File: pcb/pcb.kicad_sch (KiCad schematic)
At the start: 182 parts, among them J1 USB_C_Receptacle_USB2.0_14P, J2 Conn_01x04_Pin, J3 Conn_01x04_Pin, J4 Conn_01x04_Socket, J5 Conn_01x02_Pin, Q1 BSS84, SW1 SW_Push, SW10(8) SW_Push_45deg, SW11(9) SW_Push_45deg, SW12(0) SW_Push_45deg, SW13(-) SW_Push_45deg, SW14(=) SW_Push_45deg, SW15(bckspc) SW_Push_45deg, SW16(tab) SW_Push_45deg, SW17(q) SW_Push_45deg, SW18(w) SW_Push_45deg, SW19(e) SW_Push_45deg, SW2(esc) SW_Push_45deg, SW20(r) SW_Push_45deg, SW21(t) SW_Push_45deg, SW22(y) SW_Push_45deg, SW23(u) SW_Push_45deg, SW24(i) SW_Push_45deg, SW25(o) SW_Push_45deg, SW26(p) SW_Push_45deg, SW27([) SW_Push_45deg, SW28(]) SW_Push_45deg, SW29(\) SW_Push_45deg, SW3(1) SW_Push_45deg, SW30(caps) SW_Push_45deg, SW31(unused) SW_Push_45deg, SW32(a) SW_Push_45deg, SW33(lshift) SW_Push_45deg, SW34(s) SW_Push_45deg, SW35(z) SW_Push_45deg, SW36(d) SW_Push_45deg, SW37(x) SW_Push_45deg, SW38(f) SW_Push_45deg, SW39(c) SW_Push_45deg, SW4(2) SW_Push_45deg, SW40(g) SW_Push_45deg, SW41(v) SW_Push_45deg, SW42(h) SW_Push_45deg, SW43(b) SW_Push_45deg, SW44(j) SW_Push_45deg, SW45(n) SW_Push_45deg, SW46(k) SW_Push_45deg, SW47(m) SW_Push_45deg, SW48(l) SW_Push_45deg, SW49(,) SW_Push_45deg, SW5(3) SW_Push_45deg, SW50(;) SW_Push_45deg, SW51(.) SW_Push_45deg, SW52(') SW_Push_45deg, SW53(/) SW_Push_45deg, SW54(ret) SW_Push_45deg, SW55(rshift) SW_Push_45deg, SW56(unused) SW_Push_45deg, SW57(up) SW_Push_45deg, SW58(globe) SW_Push_45deg, SW6(4) SW_Push_45deg, SW60(lctrl) SW_Push_45deg, SW62(super) SW_Push_45deg, SW64(lalt) SW_Push_45deg, SW66(spc) SW_Push_45deg, SW68(spc) SW_Push_45deg, SW7(5) SW_Push_45deg, SW70(spc) SW_Push_45deg, SW72(spc) SW_Push_45deg, SW74(spc) SW_Push_45deg, SW76(ralt) SW_Push_45deg, SW78(rctrl) SW_Push_45deg, SW8(6) SW_Push_45deg, SW80(left) SW_Push_45deg, SW82(down) SW_Push_45deg, SW84(right) SW_Push_45deg, SW9(7) SW_Push_45deg, U1 ESP32-C3-WROOM-02, U2 AP2112K-3.3, U3 TCA6424ARGJR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

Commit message: add nc flag to nc pins on symbol and most importantly, connect all the necessary components to get the touchic funcitoning (ATMXT1664T3-CCUR035 136-ball bga version)
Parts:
- removed J3: Conn_01x04_Pin, symbol Connector:Conn_01x04_Pin
- removed SW10(8): SW_Push_45deg, symbol Switch:SW_Push_45deg
- added C10, C13, C14, C16, C6: 2.2uF, symbol Device:C
- added C11, C12, C15, C17: 22nF, symbol Device:C
- added C7, C9: 100nF, symbol Device:C
- added C8: 10nF, symbol Device:C
- added R27, R28, R29: R, symbol Device:R
- added R30: 100k, symbol Device:R
- added R31: 3.3k, symbol Device:R
- added R32: 10k, symbol Device:R
- added SW10(8)1: SW_Push_45deg, symbol Switch:SW_Push_45deg
- added SW2, SW3, SW4: SW_Push, symbol Switch:SW_Push
- added U5: ~, footprints:UFBGA136_MCH-M, symbol 2025-08-11_22-50-31:The_Touch_IC
- renumbered SW11(9) to SW11(9)1, SW12(0) to SW12(0)1, SW13(-) to SW13(-)1, SW14(=) to SW14(=)1, SW15(bckspc) to SW15(bckspc)1, SW16(tab) to SW16(tab)1, SW17(q) to SW17(q)1, SW18(w) to SW18(w)1, SW19(e) to SW19(e)1, SW2(esc) to SW2(esc)1, SW20(r) to SW20(r)1, SW21(t) to SW21(t)1, SW22(y) to SW22(y)1, SW23(u) to SW23(u)1, SW24(i) to SW24(i)1, SW25(o) to SW25(o)1, SW26(p) to SW26(p)1, SW27([) to SW27([)1, SW28(]) to SW28(])1, SW29(\) to SW29(\)1, SW3(1) to SW3(1)1, SW30(caps) to SW30(caps)1, SW31(unused) to SW31(unused)1, SW32(a) to SW32(a)1, SW33(lshift) to SW33(lshift)1, SW34(s) to SW34(s)1, SW35(z) to SW35(z)1, SW36(d) to SW36(d)1, SW37(x) to SW37(x)1, SW38(f) to SW38(f)1, SW39(c) to SW39(c)1, SW4(2) to SW4(2)1, SW40(g) to SW40(g)1, SW41(v) to SW41(v)1, SW42(h) to SW42(h)1, SW43(b) to SW43(b)1, SW44(j) to SW44(j)1, SW45(n) to SW45(n)1, SW46(k) to SW46(k)1, SW47(m) to SW47(m)1, SW48(l) to SW48(l)1, SW49(,) to SW49(,)1, SW5(3) to SW5(3)1, SW50(;) to SW50(;)1, SW51(.) to SW51(.)1, SW52(') to SW52(')1, SW53(/) to SW53(/)1, SW54(ret) to SW54(ret)1, SW55(rshift) to SW55(rshift)1, SW56(unused) to SW56(unused)1, SW57(up) to SW57(up)1, SW58(globe) to SW58(globe)1, SW6(4) to SW6(4)1, SW60(lctrl) to SW60(lctrl)1, SW62(super) to SW62(super)1, SW64(lalt) to SW64(lalt)1, SW66(spc) to SW66(spc)1, SW68(spc) to SW68(spc)1, SW7(5) to SW7(5)1, SW70(spc) to SW70(spc)1, SW72(spc) to SW72(spc)1, SW74(spc) to SW74(spc)1, SW76(ralt) to SW76(ralt)1, SW78(rctrl) to SW78(rctrl)1, SW8(6) to SW8(6)1, SW80(left) to SW80(left)1, SW82(down) to SW82(down)1, SW84(right) to SW84(right)1, SW9(7) to SW9(7)1
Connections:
- net +3.3V: now also U3.27 (VCCP), C12.1, C13.1, SW2.2, SW3.2, SW4.2, U5.N6 (VDD)
- net Column 9: now also SW10(8)1.1
- net GND: now also C10.2, C11.2, C12.2, C13.2, C14.1, C15.1, C16.1, C17.1, C6.2, C7.2, C8.2, C9.2, R27.1, R28.1, R29.1, U5.A8 (GND), U5.C1 (GND), U5.C2 (GND), U5.D11 (GND), U5.D12 (GND), U5.D3 (GND), U5.F8 (GND), U5.K5 (USB_DM), U5.K7 (GND), U5.L4 (GND), U5.L6 (COMMSEL), U5.M10 (GND), U5.M4 (GND)
- net SCL: now also U5.M5 (SCL)
- net SDA: now also U5.L5 (SDA)
- net VBUS: now also C1.1, J1.A4 (VBUS), J1.A9 (VBUS), J1.B4 (VBUS), J1.B9 (VBUS), U2.1 (VIN), U2.3 (EN)
- net at D9.2 (A): now also SW10(8)1.2
- net at U3.15 (P16): now also R29.2, SW2.1
- net at U3.16 (P17): now also R28.2, SW3.1
- net at U3.17 (P20): now also R27.2, SW4.1
- net DRV2605 renamed DRV2605_EN
- new net: C8.1, R30.2, U5.N5 (RESET#)
- new net: C10.1, C9.1, U5.D2 (VDDCORE), U5.N7 (VDDCORE)
- new net: R31.2, U5.G6 (CHG#)
- new net ADDSEL: U5.M6 (ADDSEL/USB_DP)
- new net AVDD: C14.2, C15.2, U5.D1 (AVDD), U5.D13 (AVDD), U5.E11 (AVDD), U5.E3 (AVDD), U5.N10 (AVDD), U5.N4 (AVDD)
- new net DBG_CLK: U5.L8 (DBG_CLK/XTAL_XIN)
- new net DBG_DATA: U5.H8 (DBG_DATA/XTAL_XOUT)
- new net DBG_SS#/TEST#: R32.2, U5.G8 (TEST#/DBG_SS#)
- new net DRIVEN_SHIELD: U5.H10 (DSO)
- new net GPIO0: U5.F6 (GPIO0)
- new net GPIO1: U5.M7 (GPIO1)
- new net GPIO2: U5.L7 (GPIO2)
- new net GPIO3: U5.H7 (GPIO3)
- new net GPIO4: U5.F7 (GPIO4)
- new net GPIO5: U5.M8 (GPIO5)
- new net I2C_MODE: U5.K6 (I2C_MODE)
- new net NOISE_IN: U5.H6 (NOISE_IN)
- new net VDDCORE: C6.1, C7.1
- new net VDDIO: C11.1, R30.1, R31.1, R32.1, U5.K4 (VDDIO), U5.N8 (VDDIO)
- new net VREGBOOST: U5.C13 (VREGBOOST)
- new net XVDD: C16.2, C17.2, U5.A7 (XVDD), U5.B1 (XVDD), U5.C12 (XVDD)
- no-connect marks 0 -> 1
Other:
- note added: "ATMXT1664T3-CCUR035"
- moved on the sheet: D1, D10, D11, D12, D13, D14, D15, D16, D17, D18, D19, D2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

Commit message: add all of the footprints
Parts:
- removed J1: USB_C_Receptacle_USB2.0_14P, symbol Connector:USB_C_Receptacle_USB2.0_14P
- added USB1: TYPE-C 16PIN 2MD(073), easyeda2kicad:USB-C-SMD_TYPE-C-6PIN-2MD-073, symbol easyeda2kicad:TYPE-C16PIN2MD(073)
- C1, C10, C11, C12, C13, C14, C15, C16, C17, C2, C3, C4, C5, C6, C7, C8, C9: footprint (none) -> Capacitor_SMD:C_0603_1608Metric_Pad1.08x0.95mm_HandSolder
- D1, D10, D11, D12, D13, D14, D15, D16, D17, D18, D19, D2, D20, D21, D22, D23, D24, D25, D26, D27, D28, D29, D3, D30, D31, D32, D33, D34, D35, D36, D37, D38, D39, D4, D40, D41, D42, D43, D44, D45, D46, D47, D48, D49, D5, D50, D51, D52, D53, D54, D55, D56, D57, D59, D6, D61, D63, D65, D67, D69, D7, D71, D73, D75, D77, D79, D8, D81, D83, D9: footprint (none) -> Diode_SMD:D_SOD-523
- J2, J4: footprint (none) -> Connector_PinHeader_2.54mm:PinHeader_1x04_P2.54mm_Vertical
- J5: footprint (none) -> Connector_PinHeader_2.54mm:PinHeader_1x02_P2.54mm_Vertical
- R1, R10, R11, R12, R13, R14, R15, R16, R17, R18, R19, R2, R20, R21, R22, R23, R24, R25, R26, R3, R30, R31, R32, R4, R5, R6, R7, R8, R9: footprint (none) -> Resistor_SMD:R_1206_3216Metric_Pad1.30x1.75mm_HandSolder
- R27, R28, R29: value R -> 45k; footprint (none) -> Resistor_SMD:R_1206_3216Metric_Pad1.30x1.75mm_HandSolder
- SW1, SW2, SW3, SW4: footprint (none) -> Button_Switch_THT:SW_PUSH_6mm
- SW10(8)1, SW11(9)1, SW12(0)1, SW13(-)1, SW14(=)1, SW15(bckspc)1, SW16(tab)1, SW17(q)1, SW18(w)1, SW19(e)1, SW2(esc)1, SW20(r)1, SW21(t)1, SW22(y)1, SW23(u)1, SW24(i)1, SW25(o)1, SW26(p)1, SW27([)1, SW28(])1, SW29(\)1, SW3(1)1, SW30(caps)1, SW31(unused)1, SW32(a)1, SW33(lshift)1, SW34(s)1, SW35(z)1, SW36(d)1, SW37(x)1, SW38(f)1, SW39(c)1, SW4(2)1, SW40(g)1, SW41(v)1, SW42(h)1, SW43(b)1, SW44(j)1, SW45(n)1, SW46(k)1, SW47(m)1, SW48(l)1, SW49(,)1, SW5(3)1, SW50(;)1, SW51(.)1, SW52(')1, SW53(/)1, SW54(ret)1, SW55(rshift)1, SW56(unused)1, SW57(up)1, SW58(globe)1, SW6(4)1, SW60(lctrl)1, SW62(super)1, SW64(lalt)1, SW66(spc)1, SW68(spc)1, SW7(5)1, SW70(spc)1, SW72(spc)1, SW74(spc)1, SW76(ralt)1, SW78(rctrl)1, SW8(6)1, SW80(left)1, SW82(down)1, SW84(right)1, SW9(7)1: footprint (none) -> Cherry_ULP:Cherry_ULP_TH
- U3: footprint TCA6424ARGJR:QFN50P500X500X60-33N -> library2:QFN50P500X500X60-33N
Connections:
- net D+: now also USB1.6 (DP1), USB1.8 (DP2)
- net D-: now also USB1.5 (DN2), USB1.7 (DN1)
- net GND: now also USB1.1 (GND), USB1.12 (GND), USB1.13 (SHELL), USB1.14 (SHELL)
- net VBUS: now also USB1.11 (VBUS), USB1.2 (VBUS)
- net at R2.1: now also USB1.4 (CC1)
- net at R1.1: now also USB1.10 (CC2)
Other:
- moved on the sheet: R1, R2

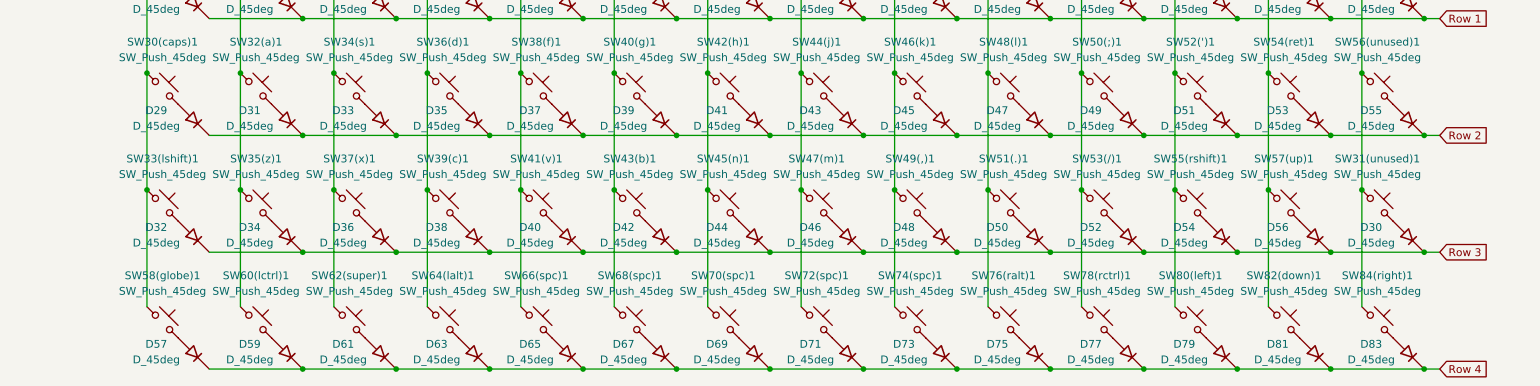
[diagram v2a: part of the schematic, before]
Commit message: arrange components for touch ic, and all keys:
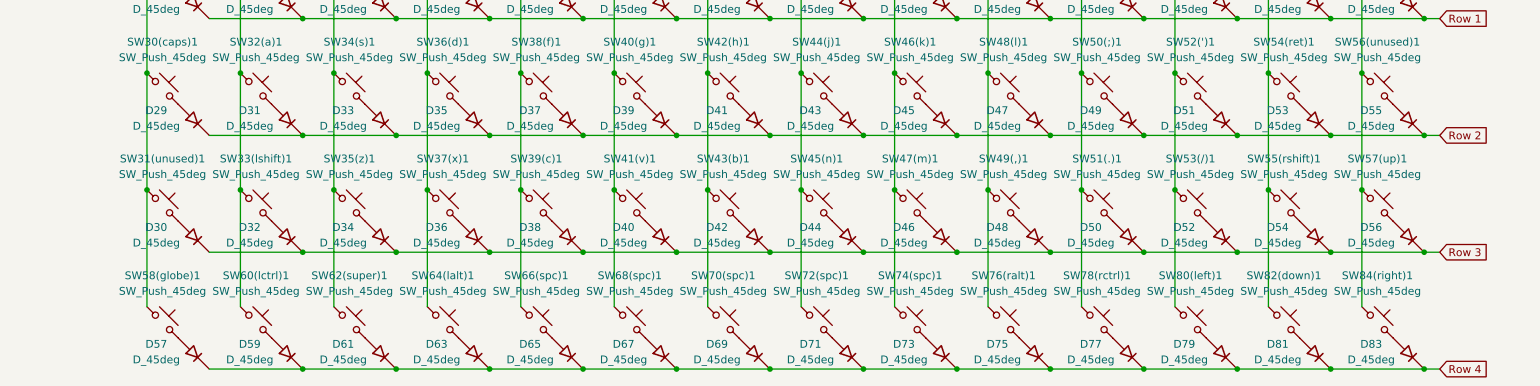
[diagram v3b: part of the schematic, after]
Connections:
- net Column 1: now also SW31(unused)1.1; no longer SW33(lshift)1.1
- net Column 10: now also SW49(,)1.1; no longer SW51(.)1.1
- net Column 11: now also SW51(.)1.1; no longer SW53(/)1.1
- net Column 12: now also SW53(/)1.1; no longer SW55(rshift)1.1
- net Column 13: now also SW55(rshift)1.1; no longer SW57(up)1.1
- net Column 14: now also SW57(up)1.1; no longer SW31(unused)1.1
- net Column 2: now also SW33(lshift)1.1; no longer SW35(z)1.1
- net Column 3: now also SW35(z)1.1; no longer SW37(x)1.1
- net Column 4: now also SW37(x)1.1; no longer SW39(c)1.1
- net Column 5: now also SW39(c)1.1; no longer SW41(v)1.1
- net Column 6: now also SW41(v)1.1; no longer SW43(b)1.1
- net Column 7: now also SW43(b)1.1; no longer SW45(n)1.1
- net Column 8: now also SW45(n)1.1; no longer SW47(m)1.1
- net Column 9: now also SW47(m)1.1; no longer SW49(,)1.1
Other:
- moved on the sheet: D30, D32, D34, D36, D38, D40, D42, D44, D46, D48, D50, D52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
